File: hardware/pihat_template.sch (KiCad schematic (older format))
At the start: 29 parts, among them P1 CONN_01X02, P2 CONN_01X02, P3 Raspberry_Pi_+_Conn, U1 LM3489, U2 CAT24C04WI-GT3, U3 FDC5614P, U4 LM1117IMPX-ADJ

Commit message: replaced r and c footprints with project:r_805 and project:c_805
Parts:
- C2, C3, C4, C5, C7, C8: footprint Capacitors_SMD:C_0805 -> project:c_0805
- JP1: footprint project:r_0603 -> project:r_0805
- R1, R10, R2, R3, R4, R5, R6, R7, R8, R9: footprint Resistors_SMD:R_0805 -> project:r_0805
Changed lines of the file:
@@
 F 0 "R1" V 2080 4650 40  0000 C CNN
 F 1 "1k" V 2007 4651 40  0000 C CNN
-F 2 "Resistors_SMD:R_0805" V 1930 4650 30  0001 C CNN
+F 2 "project:r_0805" V 1930 4650 30  0001 C CNN
 F 3 "" H 2000 4650 30  0000 C CNN
 F 4 "754-RR0510P-102D" V 2000 4650 60  0001 C CNN "Mouser Part No."
@@
 F 0 "R3" V 3930 4000 40  0000 C CNN
 F 1 "3.9k" V 3857 4001 40  0000 C CNN
-F 2 "Resistors_SMD:R_0805" V 3780 4000 30  0001 C CNN
+F 2 "project:r_0805" V 3780 4000 30  0001 C CNN
 F 3 "" H 3850 4000 30  0000 C CNN
 F 4 "71-CRCW04023K90FKED" V 3850 4000 60  0001 C CNN "Mouser Part No."
@@
 F 0 "R5" V 4180 4000 40  0000 C CNN
 F 1 "3.9k" V 4107 4001 40  0000 C CNN
-F 2 "Resistors_SMD:R_0805" V 4030 4000 30  0001 C CNN
+F 2 "project:r_0805" V 4030 4000 30  0001 C CNN
 F 3 "" H 4100 4000 30  0000 C CNN
 F 4 "71-CRCW04023K90FKED" V 4100 4000 60  0001 C CNN "Mouser Part No."
@@
 F 0 "JP1" H 1600 5350 60  0000 C CNN
 F 1 "JUMPER" H 1600 5120 40  0000 C CNN
-F 2 "project:r_0603" H 1600 5200 60  0001 C CNN
+F 2 "project:r_0805" H 1600 5200 60  0001 C CNN
 F 3 "" H 1600 5200 60  0000 C CNN
 F 4 "?" H 1600 5200 60  0001 C CNN "Farnell Part No."
@@
 F 0 "R2" V 2080 8700 40  0000 C CNN
 F 1 "24k" V 2007 8701 40  0000 C CNN
-F 2 "Resistors_SMD:R_0805" V 1930 8700 30  0001 C CNN
+F 2 "project:r_0805" V 1930 8700 30  0001 C CNN
 F 3 "" H 2000 8700 30  0000 C CNN
 F 4 "71-CRCW0402-24K-E3" V 2000 8700 60  0001 C CNN "Mouser Part No."
@@
 F 0 "C2" H 1550 9650 40  0000 L CNN
 F 1 "0.1uf" H 1556 9465 40  0000 L CNN
-F 2 "Capacitors_SMD:C_0805" H 1588 9400 30  0001 C CNN
+F 2 "project:c_0805" H 1588 9400 30  0001 C CNN
 F 3 "" H 1550 9550 60  0000 C CNN
 F 4 "810-C1005X5R1H104K" H 1550 9550 60  0001 C CNN "Mouser Part No."
@@
 F 0 "C3" H 1800 8800 40  0000 L CNN
 F 1 "1nf" H 1806 8615 40  0000 L CNN
-F 2 "Capacitors_SMD:C_0805" H 1838 8550 30  0001 C CNN
+F 2 "project:c_0805" H 1838 8550 30  0001 C CNN
 F 3 "" H 1800 8700 60  0000 C CNN
 F 4 "810-C1005C0G2A102J5C" H 1800 8700 60  0001 C CNN "Mouser Part No."
@@
 F 0 "R4" V 3980 8700 40  0000 C CNN
 F 1 "270" V 3907 8701 40  0000 C CNN
-F 2 "Resistors_SMD:R_0805" V 3830 8700 30  0001 C CNN
+F 2 "project:r_0805" V 3830 8700 30  0001 C CNN
 F 3 "" H 3900 8700 30  0000 C CNN
 F 4 "667-ERJ-P6WJ271V" V 3900 8700 60  0001 C CNN "Mouser Part No."
@@
 F 0 "R6" V 5130 8700 40  0000 C CNN
 F 1 "30k" V 5057 8701 40  0000 C CNN
-F 2 "Resistors_SMD:R_0805" V 4980 8700 30  0001 C CNN
+F 2 "project:r_0805" V 4980 8700 30  0001 C CNN
 F 3 "" H 5050 8700 30  0000 C CNN
 F 4 "594-MCT06030C3002FP5" V 5050 8700 60  0001 C CNN "Mouser Part No."
@@
 F 0 "R7" V 5130 9650 40  0000 C CNN
 F 1 "10k" V 5057 9651 40  0000 C CNN
-F 2 "Resistors_SMD:R_0805" V 4980 9650 30  0001 C CNN
+F 2 "project:r_0805" V 4980 9650 30  0001 C CNN
 F 3 "" H 5050 9650 30  0000 C CNN
 F 4 "71-CRCW0603-10K-E3" V 5050 9650 60  0001 C CNN "Mouser Part No."
@@
 F 0 "R8" V 8180 9300 50  0000 C CNN
 F 1 "390" V 8107 9301 50  0000 C CNN
-F 2 "Resistors_SMD:R_0805" V 8030 9300 30  0001 C CNN
+F 2 "project:r_0805" V 8030 9300 30  0001 C CNN
 F 3 "" H 8100 9300 30  0000 C CNN
 F 4 "594-MCT06030C3900FP5" V 8100 9300 60  0001 C CNN "Mouser Part No."
@@
 F 0 "R9" V 9230 8600 50  0000 C CNN
 F 1 "240" V 9157 8601 50  0000 C CNN
-F 2 "Resistors_SMD:R_0805" V 9080 8600 30  0001 C CNN
+F 2 "project:r_0805" V 9080 8600 30  0001 C CNN
 F 3 "" H 9150 8600 30  0000 C CNN
 F 4 "754-RR0816P-241D" V 9150 8600 60  0001 C CNN "Mouser Part No."
@@
 F 0 "R10" V 10630 9200 50  0000 C CNN
 F 1 "360" V 10557 9201 50  0000 C CNN
-F 2 "Resistors_SMD:R_0805" V 10480 9200 30  0001 C CNN
+F 2 "project:r_0805" V 10480 9200 30  0001 C CNN
 F 3 "" H 10550 9200 30  0000 C CNN
 F 4 "71-CRCW0603316RFKEB" V 10550 9200 60  0001 C CNN "Mouser Part No."
@@
 F 0 "C5" H 4800 8800 40  0000 L CNN
 F 1 "0.1uf" H 4806 8615 40  0000 L CNN
-F 2 "Capacitors_SMD:C_0805" H 4838 8550 30  0001 C CNN
+F 2 "project:c_0805" H 4838 8550 30  0001 C CNN
 F 3 "" H 4800 8700 60  0000 C CNN
 F 4 "810-C1005X5R1H104K" H 4800 8700 60  0001 C CNN "Mouser Part No."
@@
 F 0 "C7" H 9500 8650 40  0000 L CNN
 F 1 "0.1uf" H 9506 8465 40  0000 L CNN
-F 2 "Capacitors_SMD:C_0805" H 9538 8400 30  0001 C CNN
+F 2 "project:c_0805" H 9538 8400 30  0001 C CNN
 F 3 "" H 9500 8550 60  0000 C CNN
 F 4 "810-C1005X5R1H104K" H 9500 8550 60  0001 C CNN "Mouser Part No."
@@
 F 0 "C4" H 2350 4800 40  0000 L CNN
 F 1 "0.1uf" H 2356 4615 40  0000 L CNN
-F 2 "Capacitors_SMD:C_0805" H 2388 4550 30  0001 C CNN
+F 2 "project:c_0805" H 2388 4550 30  0001 C CNN
 F 3 "" H 2350 4700 60  0000 C CNN
 F 4 "810-C1005X5R1H104K" H 2350 4700 60  0001 C CNN "Mouser Part No."
@@
 F 0 "C8" H 9900 8650 40  0000 L CNN
 F 1 "1uf" H 9906 8465 40  0000 L CNN
-F 2 "Capacitors_SMD:C_0805" H 9938 8400 30  0001 C CNN
+F 2 "project:c_0805" H 9938 8400 30  0001 C CNN
 F 3 "" H 9900 8550 60  0000 C CNN
 F 4 "810-C1005X5R1H104K" H 9900 8550 60  0001 C CNN "Mouser Part No."

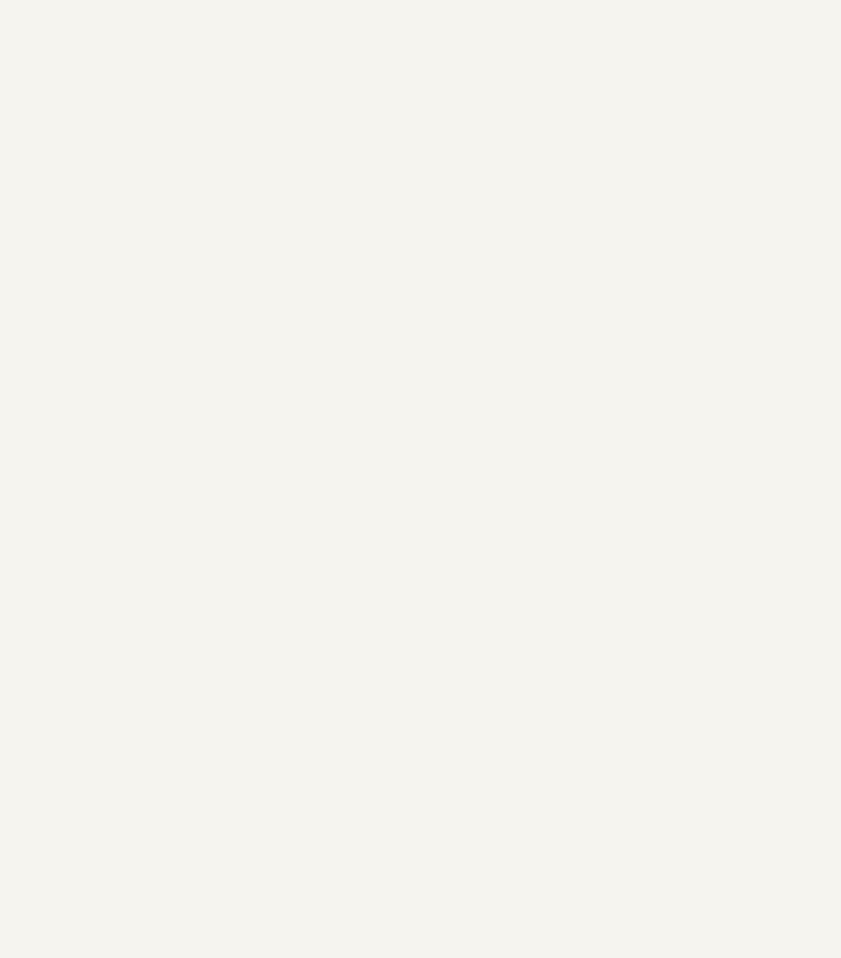
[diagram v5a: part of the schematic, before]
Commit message: Added components for serial, clock and 1-wire
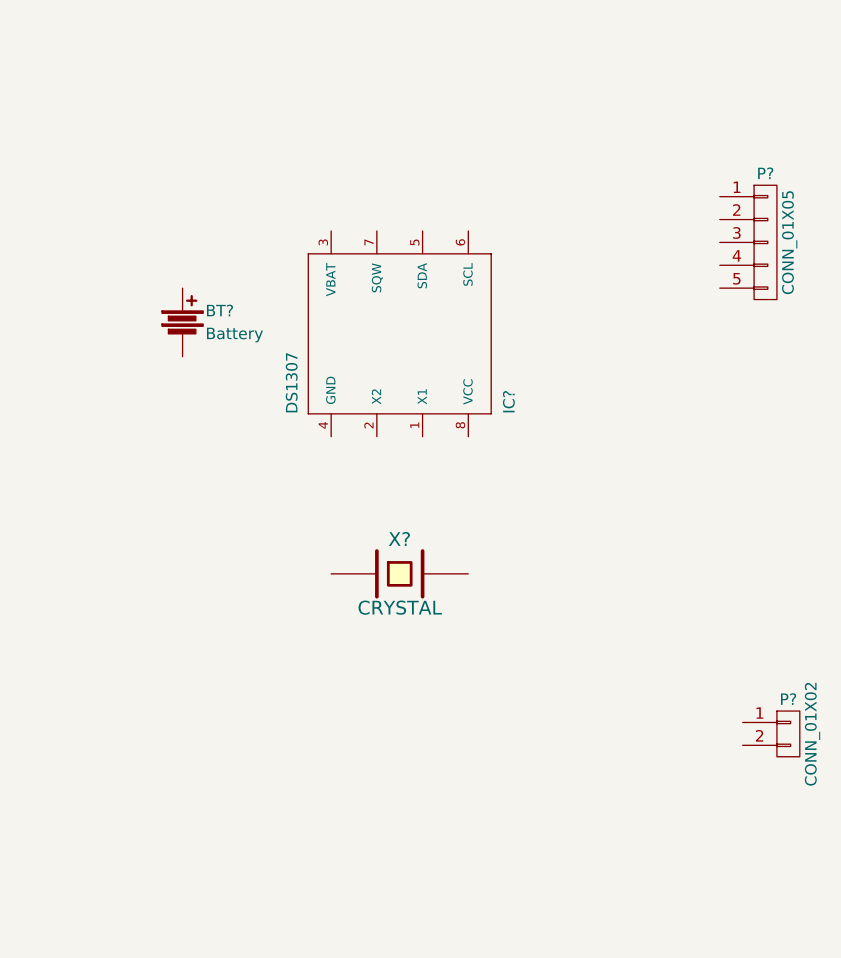
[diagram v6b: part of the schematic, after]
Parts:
- added BT?: Battery, symbol Battery
- added IC?: DS1307, ds1307_pcf8583-DIL08, symbol DS1307
- added P?: CONN_01X05, symbol CONN_01X05
- added P?: CONN_01X02, symbol CONN_01X02
- added X?: CRYSTAL, symbol CRYSTAL
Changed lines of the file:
@@
 LIBS:mcp23017
 LIBS:raspberry_pi_+_conn
+LIBS:Ardas
 LIBS:pihat_template-cache
 EELAYER 25 0
@@
 Connection ~ 1150 6850
 NoConn ~ 2100 9400
+$Comp
+L CONN_01X05 P?
+U 1 1 5A13DBD1
+P 11950 2700
+F 0 "P?" H 11950 3000 50  0000 C CNN
+F 1 "CONN_01X05" V 12050 2700 50  0000 C CNN
+F 2 "" H 11950 2700 50  0000 C CNN
+F 3 "" H 11950 2700 50  0000 C CNN
+	1    11950 2700
+	1    0    0    -1
+$EndComp
+$Comp
+L CONN_01X02 P?
+U 1 1 5A13DD6A
+P 12050 4850
+F 0 "P?" H 12050 5000 50  0000 C CNN
+F 1 "CONN_01X02" V 12150 4850 50  0000 C CNN
+F 2 "" H 12050 4850 50  0000 C CNN
+F 3 "" H 12050 4850 50  0000 C CNN
+	1    12050 4850
+	1    0    0    -1
+$EndComp
+$Comp
+L Battery BT?
+U 1 1 5A13E860
+P 9400 3050
+F 0 "BT?" H 9500 3100 50  0000 L CNN
+F 1 "Battery" H 9500 3000 50  0000 L CNN
+F 2 "" V 9400 3090 50  0000 C CNN
+F 3 "" V 9400 3090 50  0000 C CNN
+	1    9400 3050
+	1    0    0    -1
+$EndComp
+$Comp
+L CRYSTAL X?
+U 1 1 5A13EA5D
+P 10350 4150
+F 0 "X?" H 10350 4300 60  0000 C CNN
+F 1 "CRYSTAL" H 10350 4000 60  0000 C CNN
+F 2 "" H 10350 4150 60  0000 C CNN
+F 3 "" H 10350 4150 60  0000 C CNN
+	1    10350 4150
+	1    0    0    -1
+$EndComp
+$Comp
+L DS1307 IC?
+U 1 1 5A13EB02
+P 10350 3150
+F 0 "IC?" H 10050 3600 50  0000 L BNN
+F 1 "DS1307" H 10050 2650 50  0000 L BNN
+F 2 "ds1307_pcf8583-DIL08" H 10350 3300 50  0001 C CNN
+F 3 "" H 10350 3150 60  0000 C CNN
+	1    10350 3150
+	0    1    -1   0
+$EndComp
 $EndSCHEMATC

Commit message: update scheme
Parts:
- removed P?: CONN_01X05, symbol CONN_01X05
- added JP2: Jumper_NO_Small, symbol Jumper_NO_Small
- added P5: CONN_01X03, symbol CONN_01X03
- added P6: CONN_01X02, symbol CONN_01X02
- added R13, R14, R15, R16: 4,7K, symbol R
- gave numbers to parts that had none: 4
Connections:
- net +5V: now also IC1.8 (VCC), P5.1 (P1), R13.2, R14.2, R15.2, R16.1
- net GND: now also BT1.2, IC1.4 (GND), P4.2 (P2), JP2.1, P5.2 (P2)
- net PIN10: now reaches P3.10 (GPIO15/UART_RXD)
- net PIN10: now also P6.2 (P2)
- net PIN3: now reaches P3.3 (GPIO2/I2C1_SDA)
- net PIN3: now also IC1.5 (SDA), R14.1
- net PIN5: now reaches P3.5 (GPIO3/I2C1_SCL)
- net PIN5: now also IC1.6 (SCL), R15.1
- net Pin7: now reaches P3.7 (GPIO4/GPCLK0)
- net Pin7: now also P5.3 (P3), R16.2
- net PIN8: now reaches P3.8 (GPIO14/UART_TXD)
- net PIN8: now also P6.1 (P1)
- net at P4.1 (P1): now also IC1.7 (SQW), R13.1
- net at BT1.1: now also IC1.3 (VBAT), JP2.2
- net at X1.1: now also IC1.2 (X2)
- net at X1.2: now also IC1.1 (X1)
- no-connect marks 29 -> 24
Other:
- moved on the sheet: P4, X1
